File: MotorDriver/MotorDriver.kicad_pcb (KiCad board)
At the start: 2 copper layers, 70 x 70 mm, 76 parts, among them J1 Conn_01x01, J2 Conn_01x01, J3 Conn_01x01, J4 Conn_01x01, J5 Conn_02x04_Odd_Even, J6 Conn_02x03_Odd_Even, J7 4P4C, J8 4P4C, Q1 Q_NMOS_GDS, Q2 Q_NMOS_GDS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

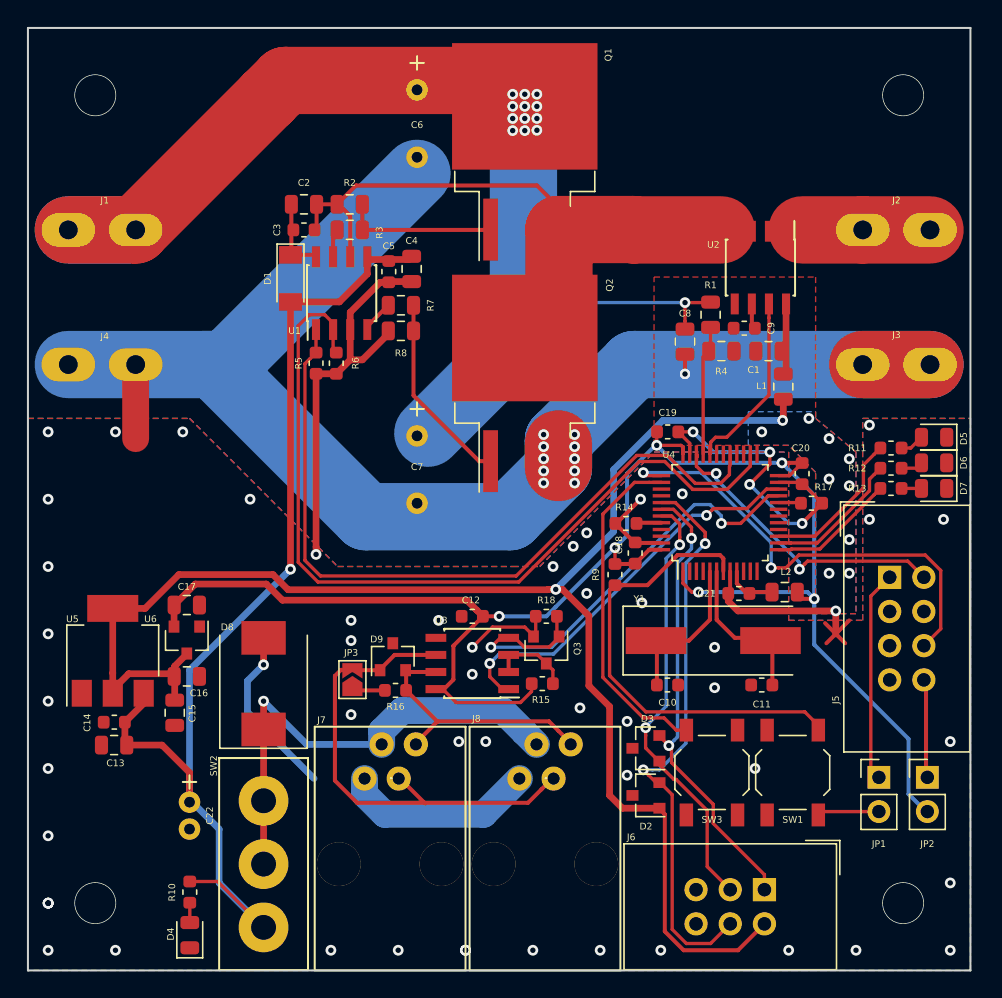
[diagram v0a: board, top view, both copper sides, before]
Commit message: First review. Fixed polygon pours, silkscreen and soldermask.
Squashed commit of the following:

commit 42a4a5d146683d2b2a8899b51cbc9eaef6797660
Author: Paweł <mackipawel@gmail.com>
Date:   Tue Apr 16 00:20:58 2019 +0200

    Changed solder mask design rules. Changed polygon pours clearence.

commit a27d25858da40b0edc55a62741cad58f571e73a1
Author: Paweł <mackipawel@gmail.com>
Date:   Sun Apr 14 15:00:25 2019 +0200

    Set via size to 0.3/0.6. Added silk screen descriptions in MotorDriver.

commit d55559f2128c74f860d75a89ad8b68139a6ba707
Author: Paweł <mackipawel@gmail.com>
Date:   Sun Apr 14 13:56:25 2019 +0200

    Added EcoTech logo in MotorController.
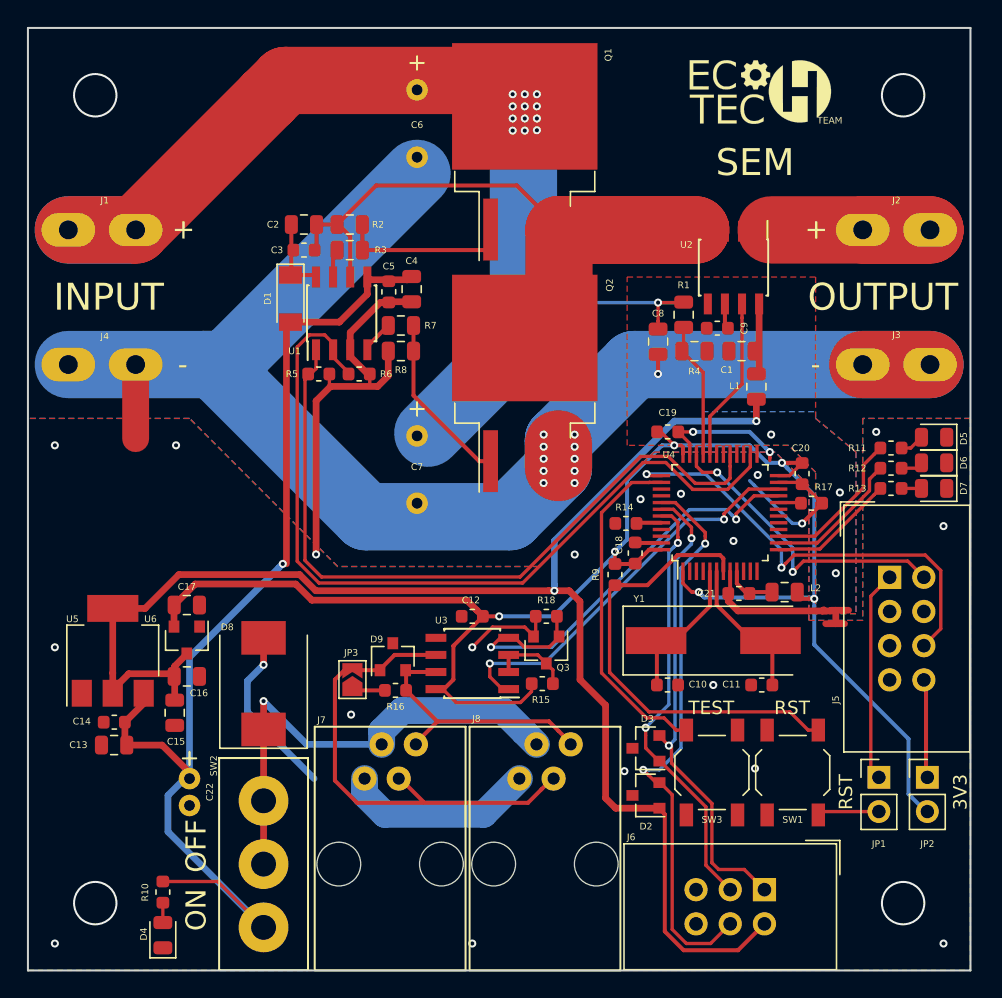
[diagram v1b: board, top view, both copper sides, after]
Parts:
- added G***: LOGO, Footprints:EcoTech, F.Cu at (154.5, 75.0)
- moved C1 2.00 mm to (153.0, 94.0)
- moved C8 2.00 mm to (146.8, 93.3)
- moved C9 2.00 mm to (151.2, 92.3)
- moved D4 2.00 mm to (110.0, 137.4)
- moved L1 2.00 mm to (154.1, 96.6)
- moved R1 2.00 mm to (148.7, 91.3)
- moved R10 2.00 mm to (110.0, 134.2)
- moved R4 2.00 mm to (149.5, 94.0)
- moved U2 2.00 mm to (152.4, 87.8)
- moved R6 1.88 mm to (124.6, 95.7), turned to 0 degrees
- moved C22 1.75 mm to (112.0, 125.8)
- moved C2 1.50 mm to (120.5, 84.6)
- moved C3 1.50 mm to (120.5, 86.5)
- moved C4 1.50 mm to (128.5, 89.4)
- moved C5 1.50 mm to (126.8, 89.6)
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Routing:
- net GND: track 208.9 -> 201.1 mm, vias 69 -> 34
- net /OUT: track 9.50 -> 16.8 mm
- net /VS: track 50.3 -> 57.1 mm
- net +5V: track 116.0 -> 114.2 mm
- net /LG: track 14.4 -> 12.9 mm
- net /ADC_I: track 13.6 -> 12.2 mm
- net /HIN: track 55.8 -> 54.6 mm
- net /ENCB: track 34.4 -> 35.5 mm
- net /SWCLK: track 34.5 -> 33.6 mm
- net /LIN: track 63.6 -> 62.7 mm
- net +3V3: track 129.0 -> 128.1 mm
- net Net-(C11-Pad1): track 11.8 -> 11.2 mm
- net /TX: track 35.5 -> 34.9 mm
- net Net-(C10-Pad1): track 11.3 -> 10.7 mm
- net /ADC_VIN: track 9.72 -> 10.3 mm
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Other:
- net class Default: via_dia 0.8 -> 0.6; via_drill 0.4 -> 0.3
- rule pad_to_mask_clearance: 0.051 -> 0.1
- rule solder_mask_min_width: 0.25 -> 0.2
- board text added: "+"
- board text added: "-"
- board text added: "3V3"
- board text added: "INPUT"
- board text added: "OFF"
- board text added: "ON"
- board text added: "OUTPUT"
- board text added: "RST"
- board text added: "SEM"
- board text added: "TEST"

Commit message: Minor changes.
Squashed commit of the following:

commit b4817053897282ec246551fcbd580ae102a3b469
Author: Paweł <mackipawel@gmail.com>
Date:   Thu Apr 25 22:57:44 2019 +0200

    Minor changes.
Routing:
- net GNDA: track 12.2 -> 14.1 mm
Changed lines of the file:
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@@
     (thickness 1.6)
     (drawings 18)
-    (tracks 609)
+    (tracks 611)
     (zones 0)
     (modules 77)
@@
   )
   (setup
-    (last_trace_width 0.25)
+    (last_trace_width 0.3)
     (user_trace_width 0.3)
     (user_trace_width 0.5)
@@
   (segment (start 160 113.25) (end 160.95 113.25) (width 0.5) (layer F.Cu) (net 6))
   (via (at 155.2 100.2) (size 0.6) (drill 0.3) (layers F.Cu B.Cu) (net 6))
+  (segment (start 150.495 92.2175) (end 150.4125 92.3) (width 0.3) (layer F.Cu) (net 6))
+  (segment (start 150.495 90.5) (end 150.495 92.2175) (width 0.3) (layer F.Cu) (net 6))
   (segment (start 128.6375 92.1) (end 128.6375 94) (width 0.3) (layer F.Cu) (net 7) (status 30))
   (segment (start 133.51 102.175) (end 134.36 102.175) (width 0.3) (layer F.Cu) (net 7))
@@
     (connect_pads (clearance 0.25))
     (min_thickness 0.25)
-    (fill yes (arc_segments 16) (thermal_gap 0.5) (thermal_bridge_width 0.5))
+    (fill yes (arc_segments 16) (thermal_gap 0.3) (thermal_bridge_width 0.4))
     (polygon
       (pts
@@
     (connect_pads (clearance 0.25))
     (min_thickness 0.25)
-    (fill yes (arc_segments 16) (thermal_gap 0.5) (thermal_bridge_width 0.5))
+    (fill yes (arc_segments 16) (thermal_gap 0.3) (thermal_bridge_width 0.4))
     (polygon
       (pts
@@
     (connect_pads (clearance 0.25))
     (min_thickness 0.25)
-    (fill yes (arc_segments 16) (thermal_gap 0.5) (thermal_bridge_width 0.5))
+    (fill yes (arc_segments 16) (thermal_gap 0.3) (thermal_bridge_width 0.4))
     (polygon
       (pts
@@
     (connect_pads (clearance 0.25))
     (min_thickness 0.25)
-    (fill yes (arc_segments 16) (thermal_gap 0.5) (thermal_bridge_width 0.5))
+    (fill yes (arc_segments 16) (thermal_gap 0.3) (thermal_bridge_width 0.4))
     (polygon
       (pts

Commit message: Removed Switches from bus devices and added mounting holes in schematics.
Squashed commit of the following:

commit 448b4f84a5f64686dc4334a0b6d81609891ca7cf
Author: Paweł <mackipawel@gmail.com>
Date:   Sun Apr 28 20:22:14 2019 +0200

    Added mouting holes to SystemSupply.

commit d45917b7024ecbe087cb8328a2c33d3ab10399ff
Author: Paweł <mackipawel@gmail.com>
Date:   Sun Apr 28 20:13:41 2019 +0200

    Added mouting holes to SafetySystem.

commit 6365380671305e2241dc821ec3b00ae08a997ac5
Author: Paweł <mackipawel@gmail.com>
Date:   Sun Apr 28 20:11:13 2019 +0200

    Added mouting holes to SafetySupply.

commit 00163d4bba61eb48f9ebb4c601b04017e78006be
Author: Paweł <mackipawel@gmail.com>
Date:   Sun Apr 28 20:06:38 2019 +0200

    Fixed MotorController.

commit ec0507ca51ef80aebbe2605505e7109beac59e98
Author: Paweł <mackipawel@gmail.com>
Date:   Sun Apr 28 19:54:40 2019 +0200

    Fixed MotorDriver.
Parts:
- removed G***: LOGO, Footprints:EcoTech
- removed NT1: Net-Tie_2, NetTie:NetTie-2_SMD_Pad0.5mm
- removed SW2: SW_SPDT, Footprints:5MS1S102AM2QE
- added G1: EcoTechLogo, Footprints:EcoTech, F.Cu at (152.2, 74.9)
- added H1: MountingHole, MountingHole:MountingHole_3.2mm_M3, F.Cu at (165.0, 75.0)
- added H2: MountingHole, MountingHole:MountingHole_3.2mm_M3, F.Cu at (105.0, 75.0)
- added H3: MountingHole, MountingHole:MountingHole_3.2mm_M3, F.Cu at (105.0, 135.0)
- added H4: MountingHole, MountingHole:MountingHole_3.2mm_M3, F.Cu at (165.0, 135.0)
- added JP4: SolderJumper_3_Open, Jumper:SolderJumper-3_P2.0mm_Open_TrianglePad1.0x1.5mm, B.Cu at (154.6, 115.0)
- added JP5: SolderJumper_3_Open, Jumper:SolderJumper-3_P2.0mm_Open_TrianglePad1.0x1.5mm, B.Cu at (159.9, 115.0)
- added JP6: SolderJumper_3_Open, Jumper:SolderJumper-3_P2.0mm_Open_TrianglePad1.0x1.5mm, B.Cu at (157.1, 115.0)
- added REF**: C_Radial_D12.5mm_H25.0mm_P5.00mm, Footprints:C_Radial_D12.5mm_H25.0mm_P5.00mm, F.Cu at (0.00, 0.00)
- J5: value Conn_02x04_Odd_Even -> Conn_02x05_Odd_Even; footprint Connector_IDC:IDC-Header_2x04_P2.54mm_Vertical -> Connector_IDC:IDC-Header_2x05_P2.54mm_Vertical
- JP2: footprint Connector_PinHeader_2.54mm:PinHeader_1x02_P2.54mm_Vertical -> Jumper:SolderJumper-2_P1.3mm_Open_TrianglePad1.0x1.5mm
- moved JP2 64.6 mm to (108.0, 99.0), turned to 270 degrees
- moved C17 10.6 mm to (119.9, 119.6), turned to 270 degrees
- moved U5 10.5 mm to (116.5, 114.1), turned to 0 degrees
- moved R10 10.0 mm to (111.7, 124.3)
- moved D4 10.0 mm to (111.7, 127.5)
- moved C13 9.59 mm to (109.5, 114.2), turned to 90 degrees
- moved C14 8.79 mm to (111.2, 114.2), turned to 90 degrees
- moved D8 8.25 mm to (116.6, 126.9), turned to 270 degrees
- moved U6 6.91 mm to (117.3, 119.6), turned to 180 degrees
- moved C22 6.89 mm to (106.1, 122.2), turned to 180 degrees
- moved R9 4.19 mm to (147.8, 110.8), turned to 180 degrees
- moved JP1 3.92 mm to (166.1, 128.3), turned to 270 degrees
- moved C16 3.18 mm to (114.6, 119.6), turned to 270 degrees
- moved R14 2.85 mm to (147.0, 105.6), turned to 90 degrees
- moved C15 2.40 mm to (111.9, 118.7), turned to 180 degrees
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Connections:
- C1 pad 2: GNDA -> GND
- C21 pad 2: GNDA -> GND
- C6 pad 2: GND -> Net-(C6-Pad2)
- C7 pad 2: GND -> Net-(C6-Pad2)
- C8 pad 2: GND -> Net-(C6-Pad2)
- C9 pad 2: GNDA -> GND
- D8 pad 1: Net-(D8-Pad1) -> +12V
- J3 pad 1: GND -> Net-(C6-Pad2)
- J4 pad 1: GND -> Net-(C6-Pad2)
- J5 pad 2: /SWDIO -> /2
- J5 pad 4: GND -> /4
- J5 pad 6: /SWCLK -> /6
- J7 pad 2: Net-(D8-Pad1) -> +12V
- J8 pad 2: Net-(D8-Pad1) -> +12V
- JP2 pad 1: Net-(J5-Pad8) -> Net-(C6-Pad2)
- JP2 pad 2: +3V3 -> GND
- Q2 pad 3: GND -> Net-(C6-Pad2)
- R4 pad 2: GNDA -> GND
- R8 pad 2: GND -> Net-(C6-Pad2)
- U2 pad 5: GNDA -> GND
- U4 pad 8: GNDA -> GND
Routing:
- net Net-(C6-Pad2): track 0.00 -> 129.3 mm, vias 0 -> 11
- net GND: track 201.1 -> 80.2 mm, vias 34 -> 29
- net Net-(D8-Pad1): track 36.4 -> 0.00 mm, vias 1 -> 0
- net +3V3: track 128.1 -> 100.8 mm
- net /4: track 0.00 -> 20.8 mm
- net /2: track 0.00 -> 18.6 mm
- net /6: track 0.00 -> 14.6 mm
- net GNDA: track 14.1 -> 0.00 mm, vias 3 -> 0
- net +12V: track 82.6 -> 96.4 mm, vias 1 -> 2
- net /SWDIO: track 22.9 -> 32.7 mm, vias 2 -> 3
- net Net-(J5-Pad1): track 16.1 -> 24.5 mm
- net Net-(J5-Pad8): track 7.51 -> 0.00 mm
- net Net-(J5-Pad5): track 0.00 -> 4.51 mm
- net +5V: track 114.2 -> 118.6 mm
- net /SWCLK: track 33.6 -> 29.3 mm, vias 2 -> 3
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- removed copper zone on B.Cu, net GNDA
- removed copper zone on F.Cu, net GNDA
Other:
- rule trace_min: 0.2 -> 0.24
- board text removed: "3V3"
- board text removed: "OFF"
- board text removed: "ON"

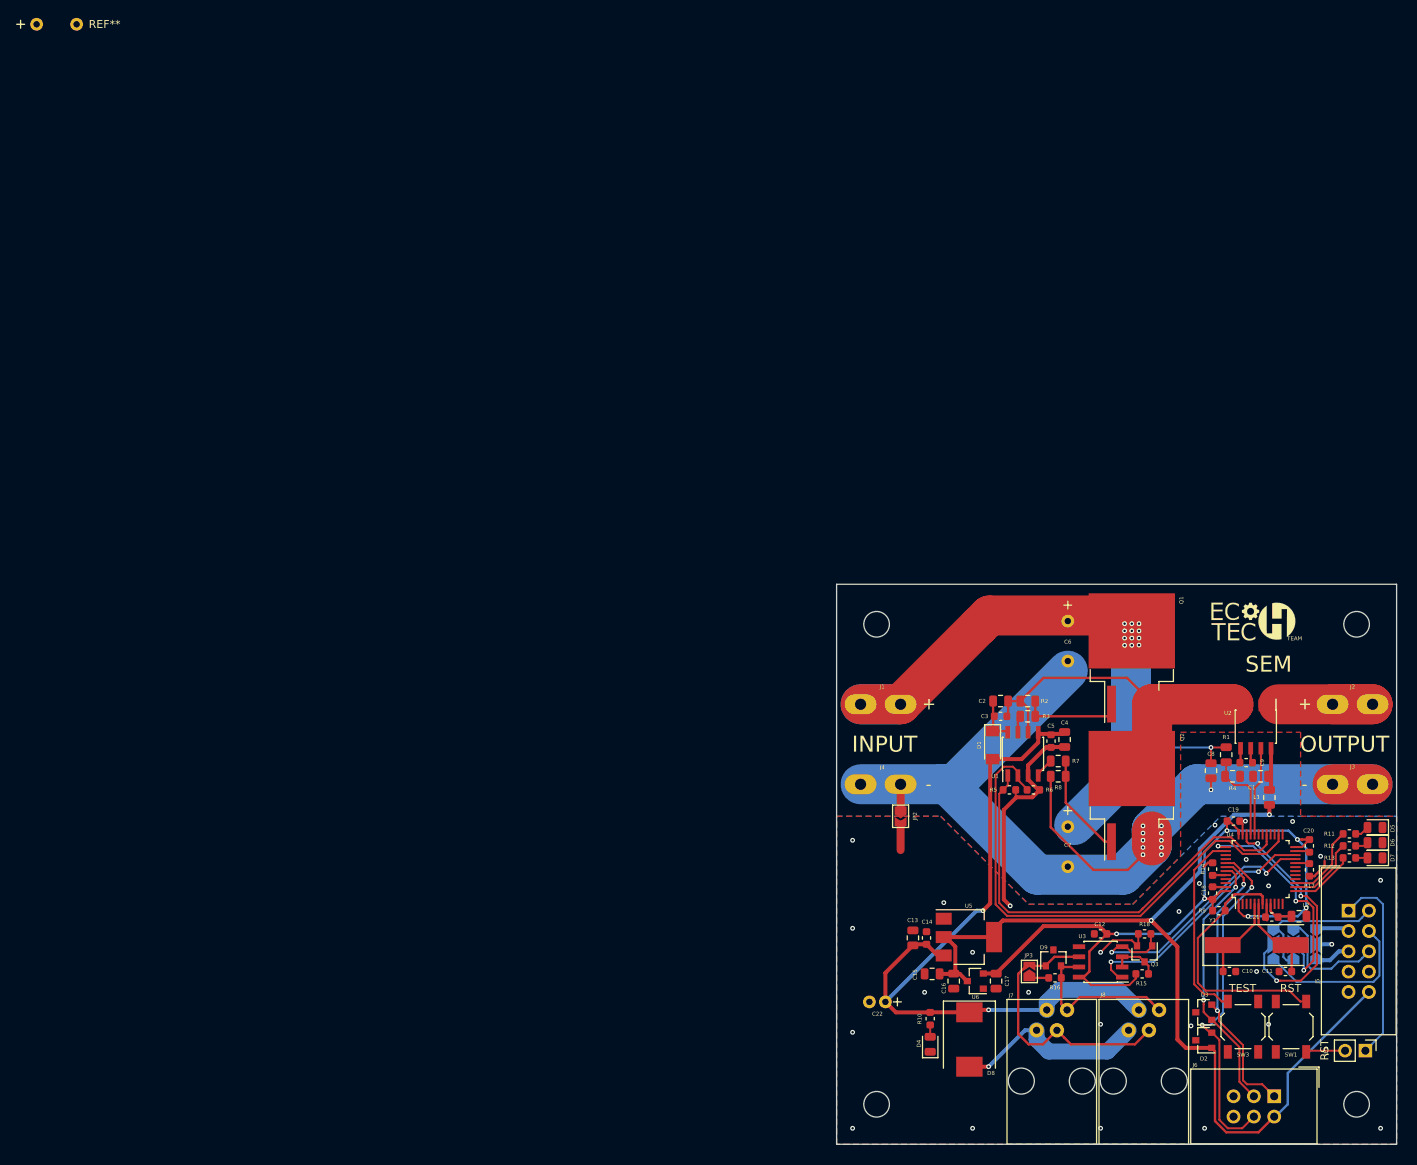
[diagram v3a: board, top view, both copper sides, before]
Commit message: Added testpoints.
Squashed commit of the following:

commit b78741095f1293168643ce5f943c13a7eb09b318
Author: Paweł <mackipawel@gmail.com>
Date:   Thu May 2 10:22:35 2019 +0200

    Added testpoints to remaining projects.

commit d708f3fd02ddff10684a41533d76b9b66ea6c8f4
Author: Paweł <mackipawel@gmail.com>
Date:   Sun Apr 28 23:49:47 2019 +0200

    Added testpoints in MotorController and MotorDriver.
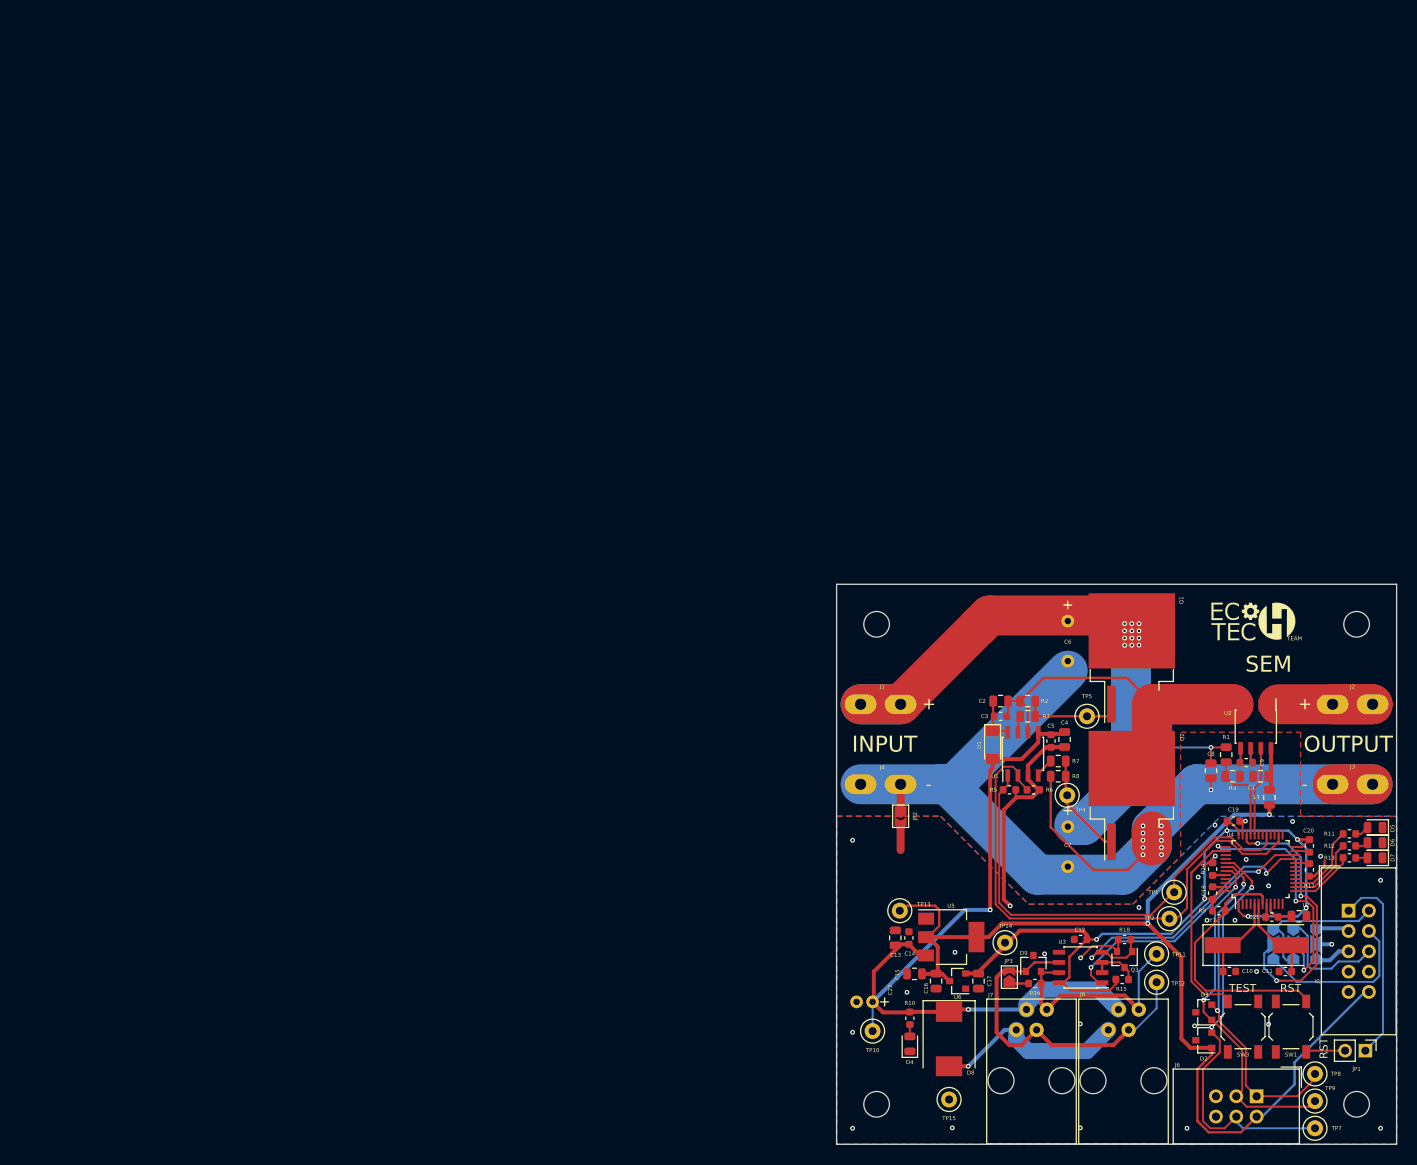
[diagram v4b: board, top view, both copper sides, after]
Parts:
- removed REF**: C_Radial_D12.5mm_H25.0mm_P5.00mm, Footprints:C_Radial_D12.5mm_H25.0mm_P5.00mm
- added TP1: TestPoint, TestPoint:TestPoint_Loop_D1.80mm_Drill1.0mm_Beaded, F.Cu at (142.2, 108.5)
- added TP10: TestPoint, TestPoint:TestPoint_Loop_D1.80mm_Drill1.0mm_Beaded, F.Cu at (104.5, 125.8)
- added TP11: TestPoint, TestPoint:TestPoint_Loop_D1.80mm_Drill1.0mm_Beaded, F.Cu at (140.0, 116.2)
- added TP12: TestPoint, TestPoint:TestPoint_Loop_D1.80mm_Drill1.0mm_Beaded, F.Cu at (140.0, 119.8)
- added TP13: TestPoint, TestPoint:TestPoint_Loop_D1.80mm_Drill1.0mm_Beaded, F.Cu at (107.9, 110.8)
- added TP14: TestPoint, TestPoint:TestPoint_Loop_D1.80mm_Drill1.0mm_Beaded, F.Cu at (121.0, 114.8)
- added TP15: TestPoint, TestPoint:TestPoint_Loop_D1.80mm_Drill1.0mm_Beaded, F.Cu at (114.1, 134.4)
- added TP2: TestPoint, TestPoint:TestPoint_Loop_D1.80mm_Drill1.0mm_Beaded, F.Cu at (141.6, 111.8)
- added TP4: TestPoint, TestPoint:TestPoint_Loop_D1.80mm_Drill1.0mm_Beaded, F.Cu at (128.8, 96.4)
- added TP5: TestPoint, TestPoint:TestPoint_Loop_D1.80mm_Drill1.0mm_Beaded, F.Cu at (131.3, 86.5)
- added TP7: TestPoint, TestPoint:TestPoint_Loop_D1.80mm_Drill1.0mm_Beaded, F.Cu at (159.8, 138.0)
- added TP8: TestPoint, TestPoint:TestPoint_Loop_D1.80mm_Drill1.0mm_Beaded, F.Cu at (159.8, 131.2)
- added TP9: TestPoint, TestPoint:TestPoint_Loop_D1.80mm_Drill1.0mm_Beaded, F.Cu at (159.8, 134.6)
- moved C12 2.60 mm to (130.5, 114.4)
- moved D9 2.60 mm to (124.6, 117.4)
- moved Q3 2.60 mm to (136.0, 116.9)
- moved R15 2.60 mm to (135.7, 119.4)
- moved R16 2.60 mm to (124.8, 119.9)
- moved R18 2.60 mm to (136.0, 114.4)
- moved U3 2.60 mm to (130.5, 117.9)
- moved JP3 2.60 mm to (121.6, 119.1)
- moved D4 2.54 mm to (109.2, 127.5)
- moved J7 2.54 mm to (124.4, 132.1)
- moved R10 2.54 mm to (109.2, 124.2)
- moved D8 2.54 mm to (114.1, 126.8)
- moved J8 2.54 mm to (135.9, 132.1)
- moved C14 2.20 mm to (109.0, 114.2)
- moved C15 2.20 mm to (109.7, 118.7)
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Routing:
- net +5V: track 118.6 -> 133.1 mm
- net /ENCA: track 33.4 -> 43.8 mm
- net /ENCI: track 43.7 -> 53.4 mm
- net /A: track 35.1 -> 43.3 mm
- net /B: track 20.9 -> 28.2 mm
- net /ENCB: track 36.5 -> 43.3 mm
- net +12V: track 96.4 -> 100.9 mm
- net /LIN: track 64.7 -> 67.8 mm
- net /TX: track 36.6 -> 39.6 mm
- net +3V3: track 100.8 -> 103.7 mm
- net /RX: track 31.3 -> 34.1 mm
- net /SWDIO: track 32.7 -> 34.8 mm
- net /SWCLK: track 29.3 -> 31.4 mm
- net /HIN: track 56.6 -> 57.8 mm
- net GND: track 80.2 -> 81.2 mm, vias 29 -> 30
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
